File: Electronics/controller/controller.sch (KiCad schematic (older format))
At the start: 13 parts, among them P1 PROMICRO_A, P2 PROMICRO_B, P3 PANEL_2, P4 PANEL_1, P5 DIAL, P6 POWER, Q1 BS107, U1 LM317T

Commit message: Updated board layout. Tidied up schematic.
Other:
- note added: "Arduino Pro Micro Headers"
- note added: "Dial Input"
- note added: "Panel Control"
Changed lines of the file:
@@
 Text Notes 1050 850  0    60   ~ 0
 Power
+Wire Notes Line
+	4250 1450 4250 3250
+Wire Notes Line
+	4250 3250 5850 3250
+Wire Notes Line
+	5850 3250 5850 1450
+Wire Notes Line
+	5850 1450 4250 1450
+Wire Notes Line
+	7050 1100 8550 1100
+Wire Notes Line
+	8550 1100 8550 2650
+Wire Notes Line
+	8550 2650 7050 2650
+Wire Notes Line
+	7050 2650 7050 1100
+Wire Notes Line
+	900  3400 3400 3400
+Wire Notes Line
+	3400 3400 3400 4850
+Wire Notes Line
+	3400 4850 900  4850
+Wire Notes Line
+	900  4850 900  3400
+Text Notes 4250 1450 0    60   ~ 0
+Panel Control
+Text Notes 7050 1100 0    60   ~ 0
+Dial Input
+Text Notes 900  3400 0    60   ~ 0
+Arduino Pro Micro Headers
 $EndSCHEMATC

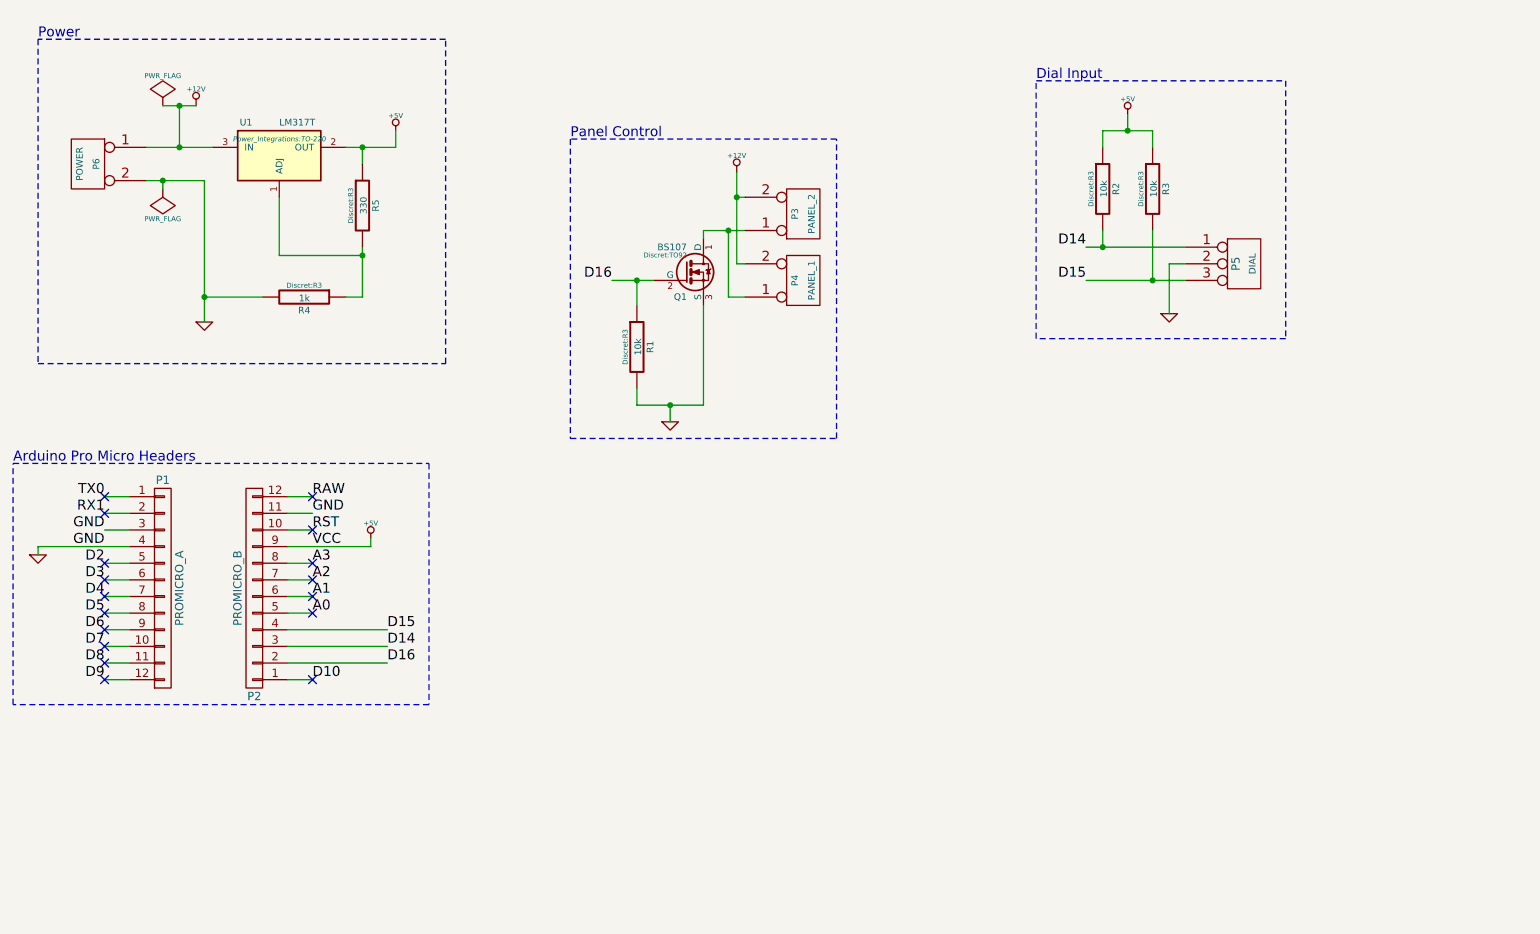
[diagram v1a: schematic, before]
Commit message: Add display driver schematic.
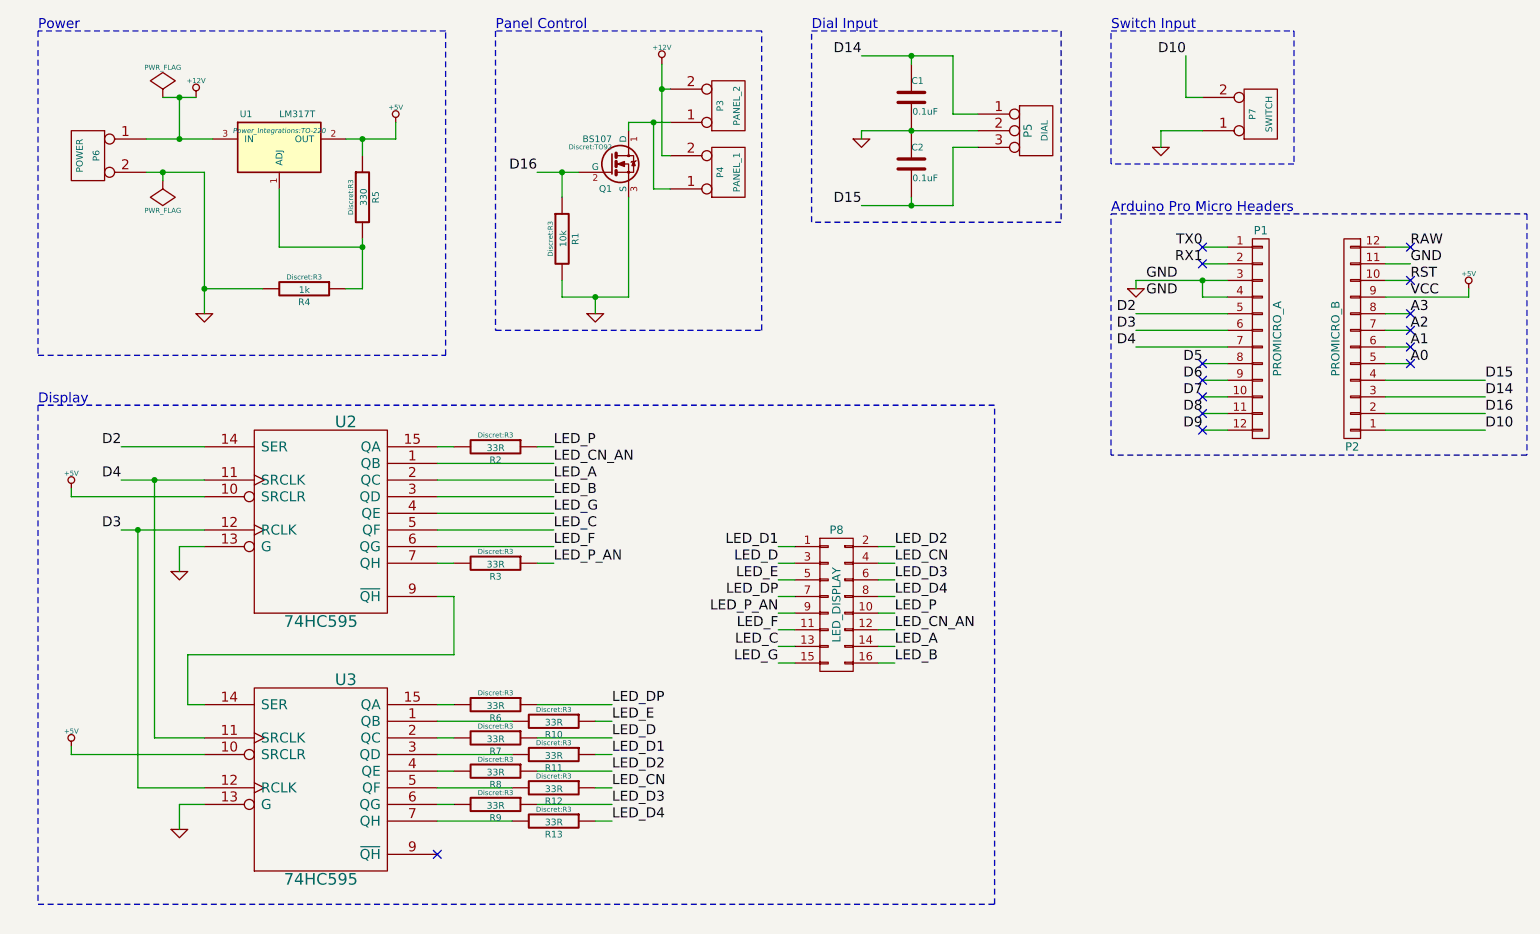
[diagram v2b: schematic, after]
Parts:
- added C1, C2: 0.1uF, Capacitors_ThroughHole:Capacitor4x3RM2.5, symbol C
- added P7: SWITCH, Connect:bornier2, symbol CONN_2
- added P8: LED_DISPLAY, Pin_Headers:Pin_Header_Straight_2x08, symbol CONN_02X08
- added R10, R11, R12, R13, R6, R7, R8, R9: 33R, Discret:R3, symbol R
- added U2, U3: 74HC595, Sockets_DIP:DIP-16__300, symbol 74HC595
- R2, R3: value 10k -> 33R
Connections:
- net +5V: now also U2.10 (SRCLR), U2.16 (VCC), U3.10 (SRCLR), U3.16 (VCC); no longer R2.1, R3.1
- net D10: now also P7.2 (P2)
- net D14: now also C1.1; no longer R2.2
- net D15: now also C2.2; no longer R3.2
- net D2: now also U2.14 (SER)
- net D3: now also U2.12 (RCLK), U3.12 (RCLK)
- net D4: now also U2.11 (SRCLK), U3.11 (SRCLK)
- net GND: now also C1.2, C2.1, P7.1 (P1), U2.13 (G), U2.8 (GND), U3.13 (G), U3.8 (GND)
- new net: R2.2, U2.15 (QA)
- new net: R3.2, U2.7 (QH)
- new net: U2.9 (~QH), U3.14 (SER)
- new net: R10.2, U3.1 (QB)
- new net: R6.2, U3.15 (QA)
- new net: R7.2, U3.2 (QC)
- new net: R11.2, U3.3 (QD)
- new net: R8.2, U3.4 (QE)
- new net: R12.2, U3.5 (QF)
- new net: R9.2, U3.6 (QG)
- new net: R13.2, U3.7 (QH)
- new net LED_A: P8.14 (P14), U2.2 (QC)
- new net LED_B: P8.16 (P16), U2.3 (QD)
- new net LED_C: P8.13 (P13), U2.5 (QF)
- new net LED_CN: P8.4 (P4), R12.1
- new net LED_CN_AN: P8.12 (P12), U2.1 (QB)
- new net LED_D: P8.3 (P3), R7.1
- new net LED_D1: P8.1 (P1), R11.1
- new net LED_D2: P8.2 (P2), R8.1
- new net LED_D3: P8.6 (P6), R9.1
- new net LED_D4: P8.8 (P8), R13.1
- new net LED_DP: P8.7 (P7), R6.1
- new net LED_E: P8.5 (P5), R10.1
- new net LED_F: P8.11 (P11), U2.6 (QG)
- new net LED_G: P8.15 (P15), U2.4 (QE)
- new net LED_P: P8.10 (P10), R2.1
- new net LED_P_AN: P8.9 (P9), R3.1
- no-connect marks 17 -> 14
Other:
- note added: "Display"
- note added: "Switch Input"
- moved on the sheet: P1, P2, P3, P4, P5, P6, Q1, R1, R4, R5, U1

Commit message: Totally broken display.
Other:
- note added: "DS"
- note added: "SH_CP"
- note added: "ST_CP"
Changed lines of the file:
@@
 LIBS:valves
 LIBS:borniers
-LIBS:components
 LIBS:controller-cache
 EELAYER 25 0
@@
 Text Notes 1050 3050 0    60   ~ 0
 Display
+Text Notes 2050 3300 2    60   ~ 0
+DS
+Text Notes 2050 3500 2    60   ~ 0
+SH_CP
+Text Notes 2050 3800 2    60   ~ 0
+ST_CP
 $EndSCHEMATC

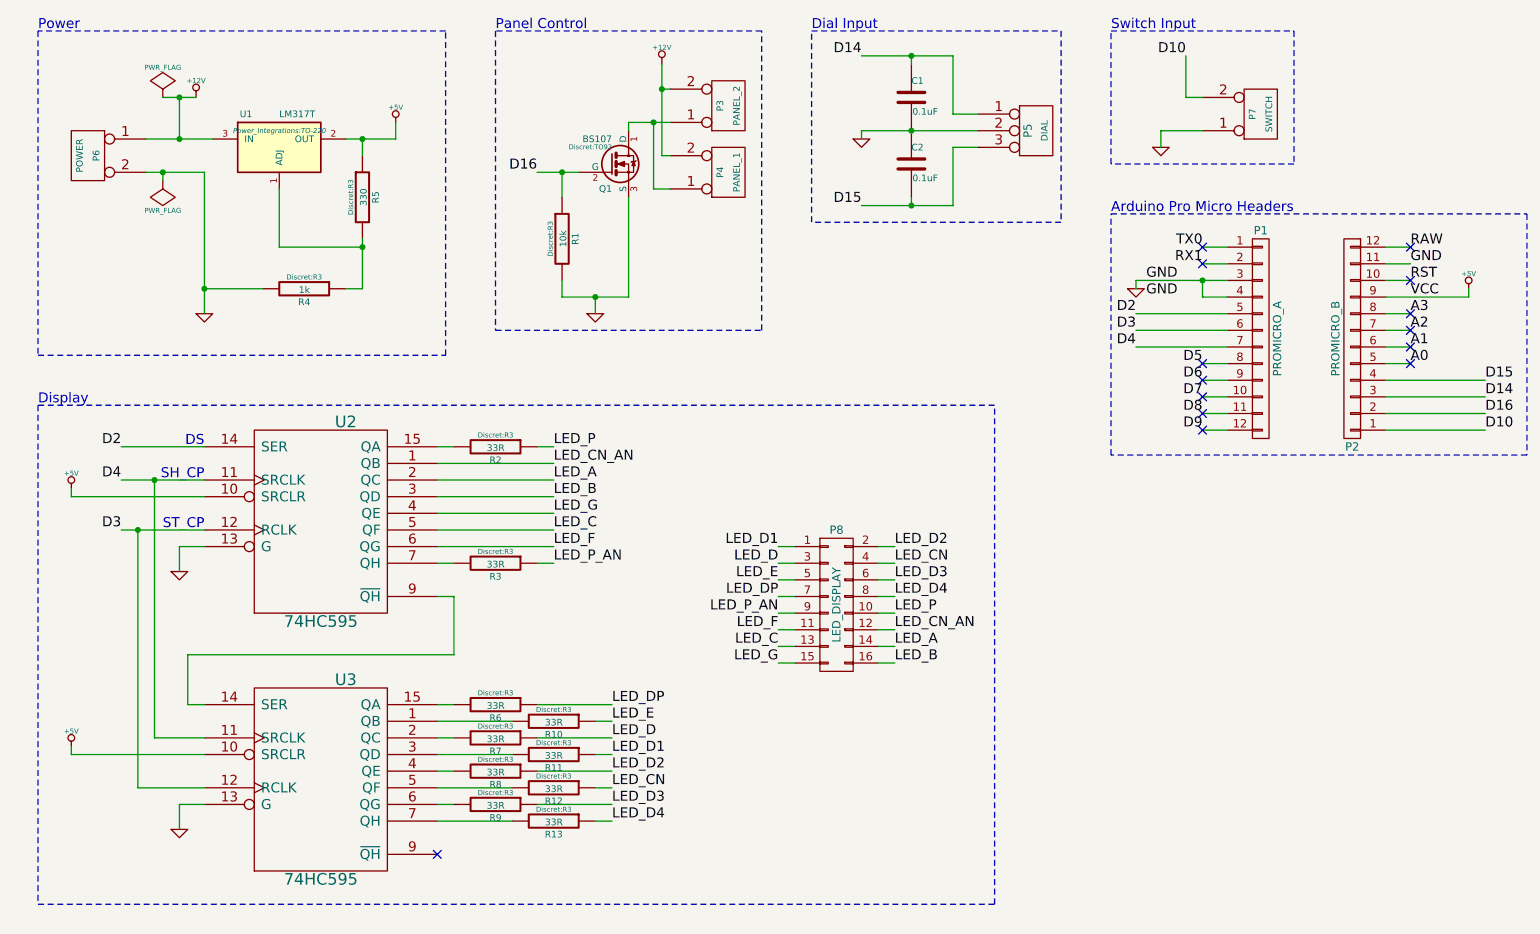
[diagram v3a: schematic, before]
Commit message: Update schematics with new single-SIPO implementation.
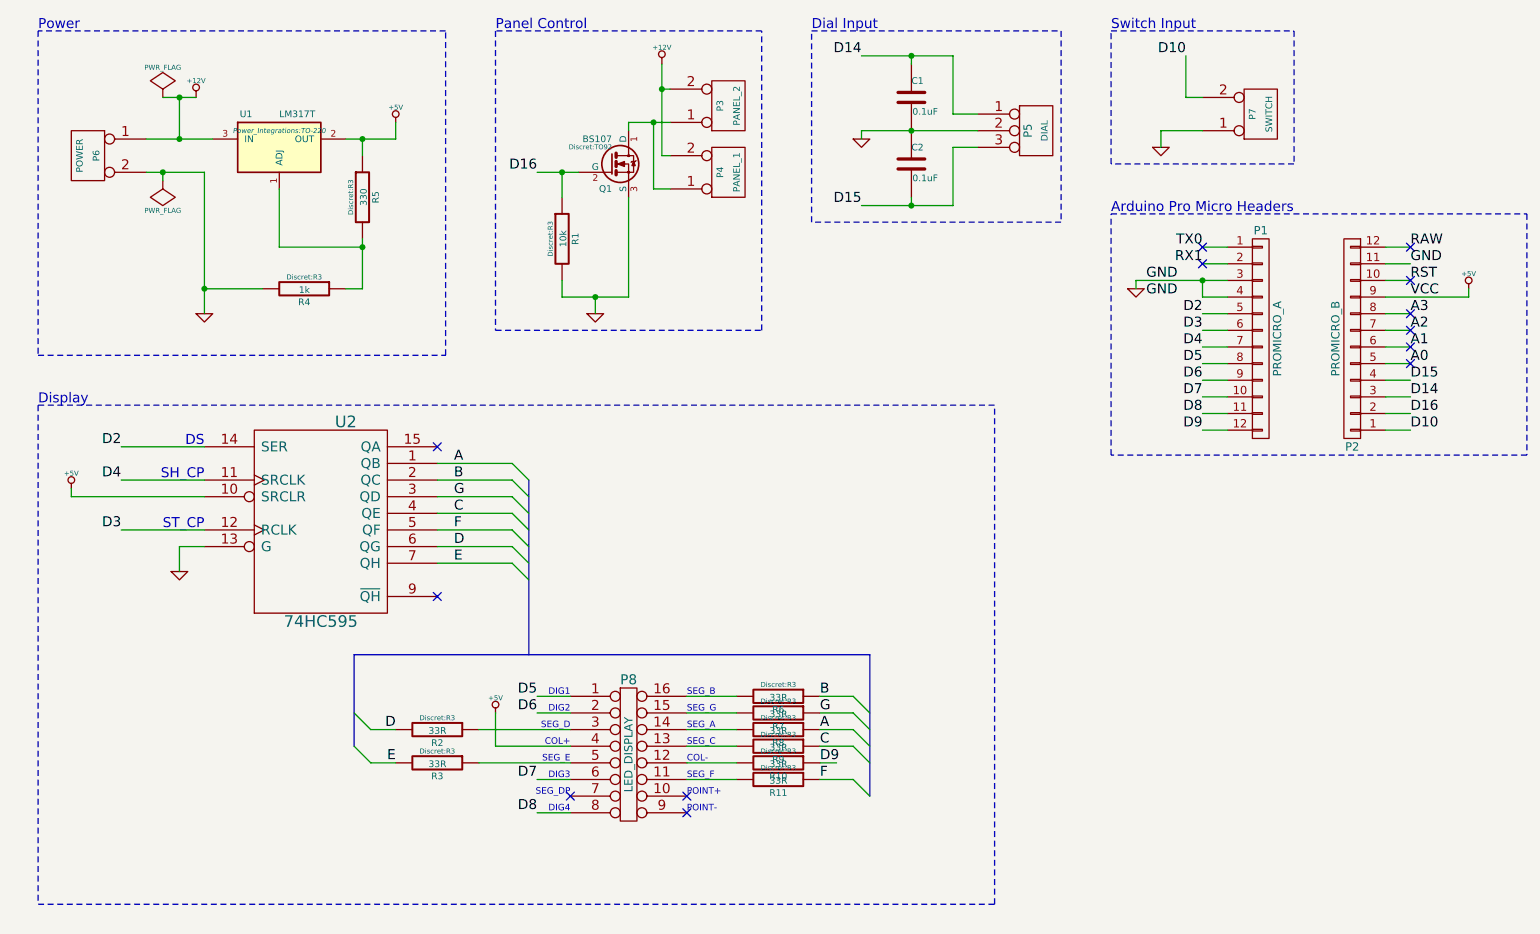
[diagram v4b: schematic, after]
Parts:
- removed P8: LED_DISPLAY, Pin_Headers:Pin_Header_Straight_2x08, symbol CONN_02X08
- removed R12, R13: 33R, Discret:R3, symbol R
- removed U3: 74HC595, Sockets_DIP:DIP-16__300, symbol 74HC595
- added P8: LED_DISPLAY, symbol DIL16
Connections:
- net LED_D is gone; now on net G: R7.1
- net LED_D1 is gone; now on net F: R11.1
- net LED_D2 is gone; now on net A: R8.1
- net LED_DP is gone; now on net B: R6.1
- net LED_E is gone; now on net D9: R10.1
- net LED_G is gone; now on net C: U2.4 (QE)
- net +5V: now also P8.4
- net D5: now also P8.1
- net D6: now also P8.2
- net D7: now also P8.6
- net D8: now also P8.8
- net at U2.15 (QA): no longer R2.2
- net E: now reaches R3.2, U2.7 (QH)
- net at R10.2: now also P8.12
- net at R6.2: now also P8.16
- net at R7.2: now also P8.15
- net at R11.2: now also P8.11
- net at R8.2: now also P8.14
- net at R9.2: now also P8.13
- net LED_A renamed B
- net LED_B renamed G
- net LED_C renamed F
- net LED_CN_AN renamed A
- net LED_D3 renamed C
- net LED_F renamed D
- net D: now also R2.2
- net LED_P: no longer names the net of R2.1
- net LED_P: now also P8.3
- net LED_P_AN: no longer names the net of R3.1
- net LED_P_AN: now also P8.5
- no-connect marks 14 -> 13
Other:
- note added: "COL+"
- note added: "COL-"
- note added: "DIG1"
- note added: "DIG2"
- note added: "DIG3"
- note added: "DIG4"
- note added: "POINT+"
- note added: "POINT-"
- note added: "SEG_A"
- note added: "SEG_B"
- note added: "SEG_C"
- note added: "SEG_D"
- note added: "SEG_DP"
- note added: "SEG_E"
- note added: "SEG_F"
- note added: "SEG_G"
- moved on the sheet: R2, R3

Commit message: Fix layout.
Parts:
- removed P1: PROMICRO_A, Pin_Headers:Pin_Header_Straight_1x12, symbol CONN_01X12
- removed P2: PROMICRO_B, Pin_Headers:Pin_Header_Straight_1x12, symbol CONN_01X12
- removed Q1: BS107, Discret:TO92, symbol BS107
- added Q1: BUZ11, Transistors_TO-220:TO-220_FET-GDS_Vertical, symbol MOSFET_N
- added U3: Arduino_Pro_Micro, Cylindric:ArduinoProMicro, symbol Arduino_Pro_Micro
- P8: footprint (none) -> Pin_Headers:Pin_Header_Straight_2x08
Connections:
- net +12V: now also P6.2 (P2); no longer P6.1 (P1)
- net D10: now also U3.13 (D10)
- net D14: now also U3.15 (D14)
- net D15: now also U3.16 (D15)
- net D16: now also Q1.G, U3.14 (D16)
- net D2: now also U3.5 (D2)
- net D3: now also U3.6 (D3)
- net D4: now also U3.7 (D4)
- net D5: now also U3.8 (D5)
- net D6: now also U3.9 (D6)
- net D7: now also U3.10 (D7)
- net D8: now also U3.11 (D8)
- net D9: now also U3.12 (D9)
- net GND: now also P6.1 (P1), Q1.S, U3.23 (GND), U3.3 (GND), U3.4 (GND); no longer P6.2 (P2)
- net at P3.1 (P1), P4.1 (P1): now also Q1.D
- net +5V renamed VCC
- net VCC: now also U3.21 (VCC)
